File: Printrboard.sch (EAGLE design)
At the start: 129 parts, among them J1 MICROSD, J3 USB-MICRO-PTH, J4 PCIE, Q1 RFP30N06LE, Q2 RFP30N06LE, Q3 RFP30N06LE, Q4 RFP30N06LE, U1 LM2841, U10 MCP4728, U2 A4982, U3 A4982, U4 A4982, U5 A4982, U6 AT90USB1286, U7 AP7313, U8 TXB0104, U9 PRTR5V0U4D, X1 16MHz

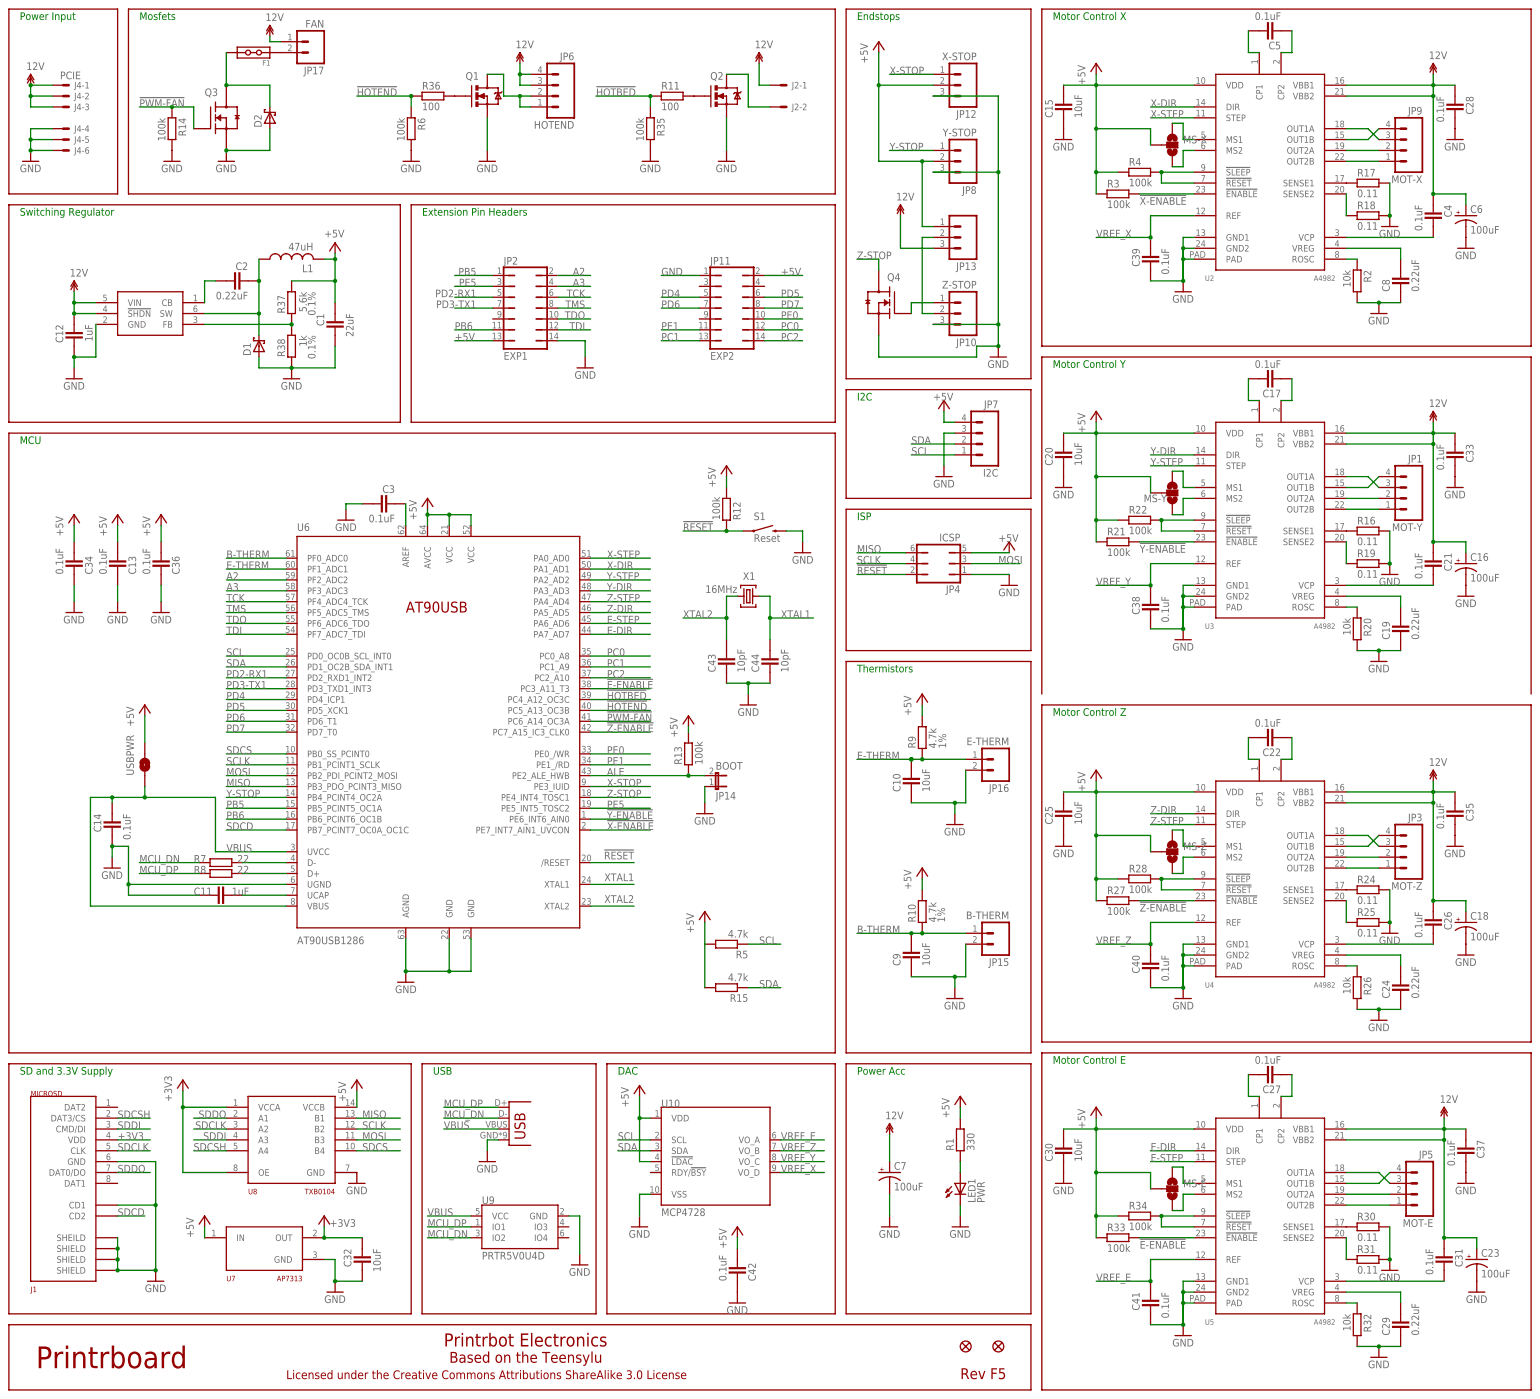
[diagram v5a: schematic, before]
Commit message: Rev F6
Add second Fan port
Add optional USB-B footprint
Remove polyswitch
Change to push-push microSD socket
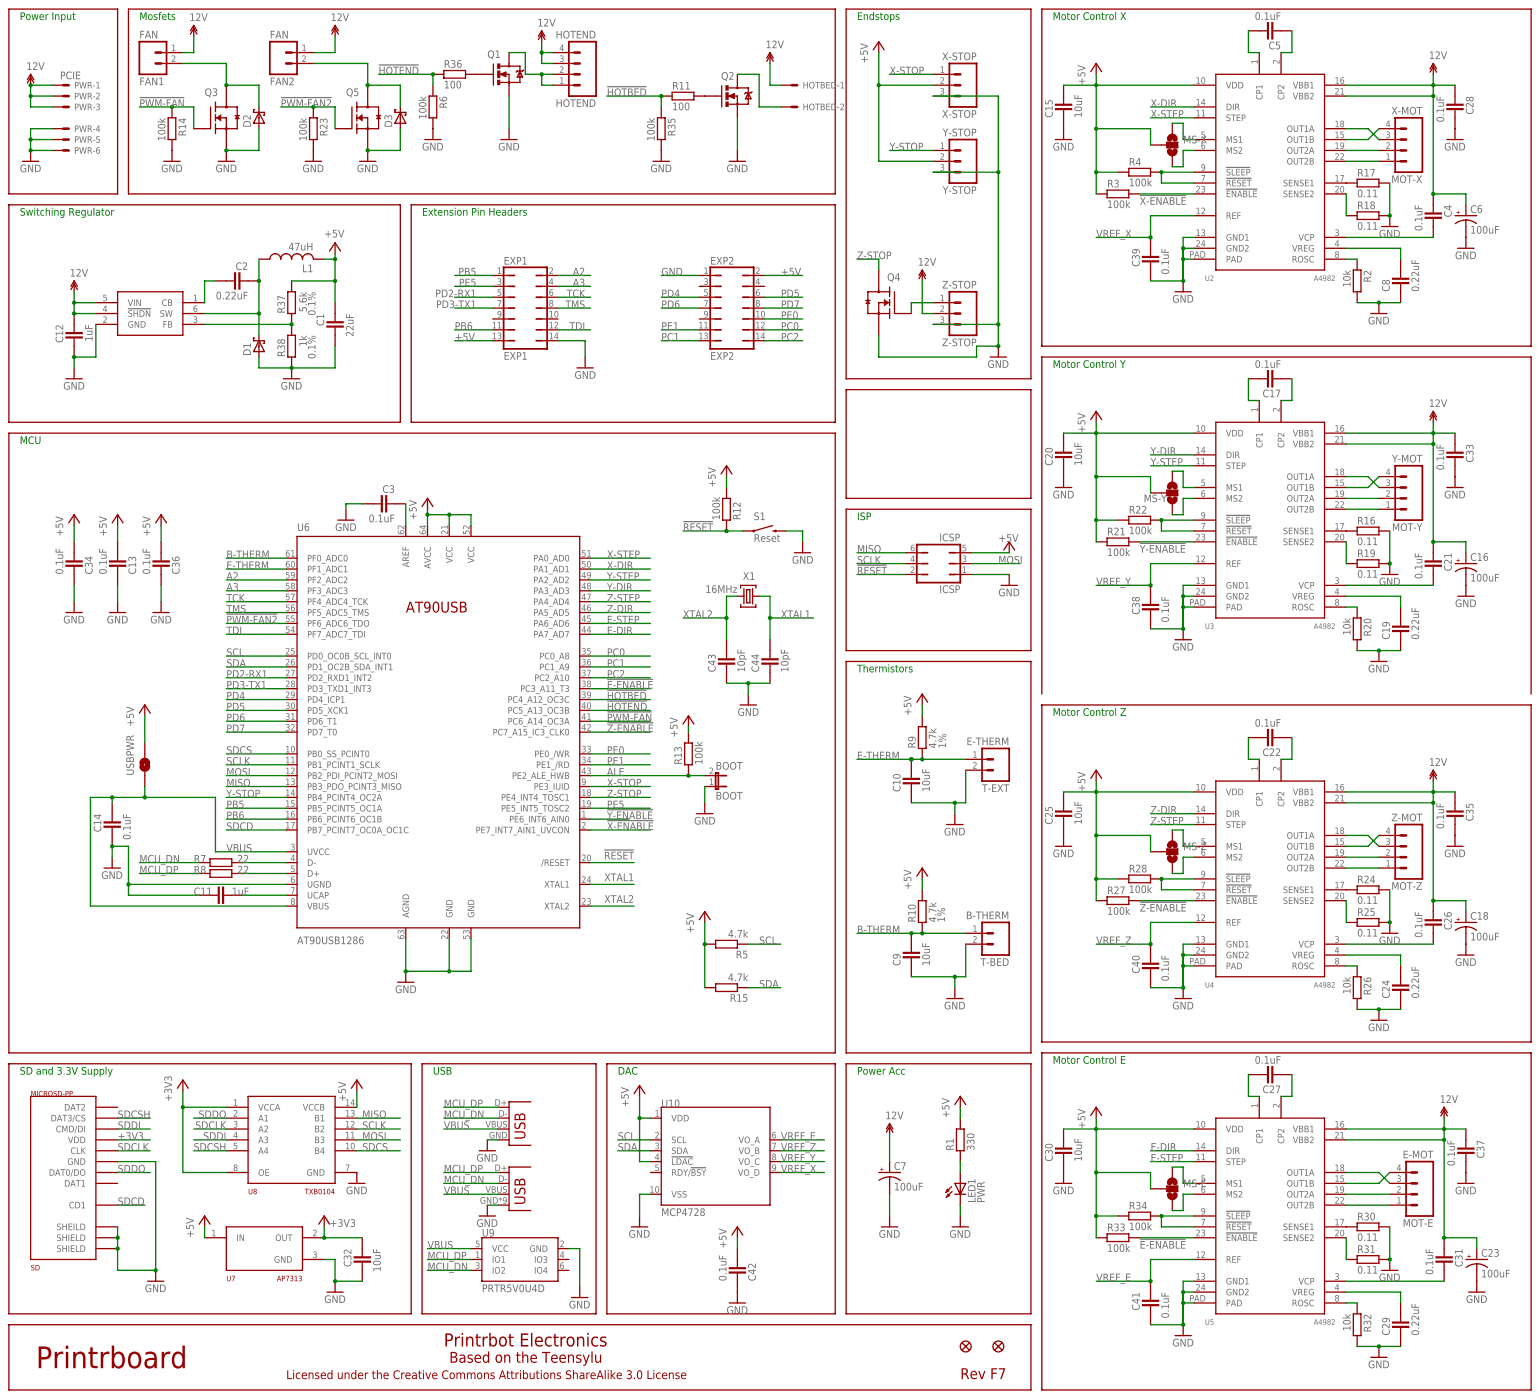
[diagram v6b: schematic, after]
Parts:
- removed F1: MINISMDC050F, printrbot:MINISMDC050F
- removed J1: MICROSD, printrbot:MICROSD
- removed J2: (no value), printrbot:PHOENIX-2POS-5MM-SCREW
- removed J3: USB-MICRO-PTH, printrbot:USB-MICRO-PTH
- removed JP13: (no value), SparkFun:M03PTH
- removed JP17: FAN, SparkFun:M02PTH
- removed JP6: HOTEND, SparkFun:M04POLAR
- removed JP7: I2C, SparkFun:M04POLAR
- added D3: SCH-DIODESMA, printrbot:SCH-DIODESMA
- added FAN1, FAN2: FAN, SparkFun:M02PTH
- added HOTBED: (no value), printrbot:PHOENIX-2POS-5MM-SCREW
- added HOTEND: HOTEND, SparkFun:M04POLAR
- added Q5: RFP30N06LE, ipc-7351-transistor:MOSFET-NCH_SOT-23
- added R23: 100k, ipc-7351-resistor:RESISTOR_0805
- added SD: MICROSD-PP, printrbot:MICROSD-PP
- added USB-B: USBPTH, printrbot:USBPTH
- added USB-M: USB-MICRO-PTH, printrbot:USB-MICRO-PTH
- renumbered J4 to PWR, JP1 to Y-MOT, JP10 to Z-STOP, JP11 to EXP2, JP12 to X-STOP, JP14 to BOOT, JP15 to T-BED, JP16 to T-EXT, JP2 to EXP1, JP3 to Z-MOT, JP4 to ICSP, JP5 to E-MOT, JP8 to Y-STOP, JP9 to X-MOT
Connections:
- removed net N$5: F1.P$1, JP17.2
- removed net TDO: EXP1.10, U6.PF6_ADC6_TDO
- new net !PWM-FAN2: Q5.G, R23.1, U6.PF6_ADC6_TDO
- net +3V3: now also SD.VDD; no longer J1.VDD
- net +5V: no longer JP13.1, JP7.4
- net 12V: now also FAN1.1, FAN2.1, HOTBED-1.S, HOTEND.3, HOTEND.4, Z-STOP.2; no longer J2-1.S, JP13.3, JP17.1, JP6.3, JP6.4
- net GND: now also D3.A, Q5.S, R23.2, SD.GND, SD.SHEILD@1, SD.SHIELD@2, SD.SHIELD@3, USB-B.GND, USB-M.GND; no longer J1.CD1, J1.GND, J1.SHEILD@1, J1.SHIELD@2, J1.SHIELD@3, J1.SHIELD@4, J3.GND, JP7.3
- net HOTBED-GND: now also HOTBED-2.S; no longer J2-2.S
- net HOTEND-GND: now also HOTEND.1, HOTEND.2; no longer JP6.1, JP6.2
- net MCU_DN: now also USB-B.D-, USB-M.D-; no longer J3.D-
- net MCU_DP: now also USB-B.D+, USB-M.D+; no longer J3.D+
- net N$2: now also FAN1.2; no longer F1.P$2
- net N$8: now also D3.C, FAN2.2, Q5.D; no longer JP13.2, Z-STOP.2
- net SCL: no longer JP7.1
- net SDA: no longer JP7.2
- net SDCD: now also SD.CD1; no longer J1.CD2
- net SDCLK: now also SD.CLK; no longer J1.CLK
- net SDCSH: now also SD.DAT3/CS; no longer J1.DAT3/CS
- net SDDI: now also SD.CMD/DI; no longer J1.CMD/DI
- net SDDO: now also SD.DAT0/DO; no longer J1.DAT0/DO
- net VBUS: now also USB-B.VBUS, USB-M.VBUS; no longer J3.VBUS
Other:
- note added: "Rev F7"
- note removed: "I2C"
- note removed: "Rev F5"
- moved on the sheet: D2, Q1, Q2, R11, R35, R36, R6, U9

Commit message: Add in changes requested by PBHQ
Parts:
- removed USB-B: USBPTH, printrbot:USBPTH
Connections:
- net GND: no longer USB-B.GND
- net MCU_DN: no longer USB-B.D-
- net MCU_DP: no longer USB-B.D+
- net VBUS: no longer USB-B.VBUS
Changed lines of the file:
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@@
 <part name="U9" library="printrbot" deviceset="PRTR5V0U4D" device=""/>
 <part name="GND53" library="SparkFun" deviceset="GND" device=""/>
-<part name="GND54" library="SparkFun" deviceset="GND" device=""/>
 <part name="U10" library="printrbot" deviceset="MCP4728" device=""/>
 <part name="GND56" library="SparkFun" deviceset="GND" device=""/>
@@
 <part name="Q4" library="ipc-7351-transistor" deviceset="MOSFET-NCH_" device="SOT-23" value="RFP30N06LE"/>
 <part name="U$6" library="12v" deviceset="12V" device=""/>
-<part name="USB-B" library="printrbot" deviceset="USB" device="PTH"/>
 <part name="SD" library="printrbot" deviceset="MICROSD-PP" device=""/>
 <part name="R23" library="ipc-7351-resistor" deviceset="RESISTOR_" device="0805" value="100k"/>
@@
 <instance part="U9" gate="G$1" x="119.38" y="-50.8"/>
 <instance part="GND53" gate="1" x="133.35" y="-59.69"/>
-<instance part="GND54" gate="1" x="111.76" y="-25.4"/>
 <instance part="U10" gate="G$1" x="165.1" y="-25.4"/>
 <instance part="GND56" gate="1" x="147.32" y="-43.18"/>
@@
 </instance>
 <instance part="U$6" gate="G$1" x="213.36" y="177.8"/>
-<instance part="USB-B" gate="G$1" x="116.84" y="-22.86"/>
 <instance part="SD" gate="G$1" x="12.7" y="-33.02"/>
 <instance part="R23" gate="G$1" x="71.12" y="213.36" rot="R270"/>
@@
 </segment>
 <segment>
-<wire x1="114.3" y1="-22.86" x2="111.76" y2="-22.86" width="0.1524" layer="91"/>
-<pinref part="GND54" gate="1" pin="GND"/>
-<pinref part="USB-B" gate="G$1" pin="GND"/>
-</segment>
-<segment>
 <pinref part="U10" gate="G$1" pin="VSS"/>
 <pinref part="GND56" gate="1" pin="GND"/>
@@
 </segment>
 <segment>
-<wire x1="114.3" y1="-17.78" x2="101.6" y2="-17.78" width="0.1524" layer="91"/>
-<label x="101.6" y="-17.78" size="1.778" layer="95"/>
-<pinref part="USB-B" gate="G$1" pin="D-"/>
-</segment>
-<segment>
 <pinref part="U9" gate="G$1" pin="IO2"/>
 <wire x1="107.95" y1="-53.34" x2="97.79" y2="-53.34" width="0.1524" layer="91"/>
@@
 <pinref part="R8" gate="G$1" pin="1"/>
 <label x="30.48" y="39.37" size="1.778" layer="95"/>
-</segment>
-<segment>
-<wire x1="114.3" y1="-15.24" x2="101.6" y2="-15.24" width="0.1524" layer="91"/>
-<label x="101.6" y="-15.24" size="1.778" layer="95"/>
-<pinref part="USB-B" gate="G$1" pin="D+"/>
 </segment>
 <segment>
@@
 </segment>
 <segment>
-<wire x1="114.3" y1="-20.32" x2="101.6" y2="-20.32" width="0.1524" layer="91"/>
-<label x="101.6" y="-20.32" size="1.778" layer="95"/>
-<pinref part="USB-B" gate="G$1" pin="VBUS"/>
-</segment>
-<segment>
